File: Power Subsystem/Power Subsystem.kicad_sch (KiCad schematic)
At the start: 8 parts, among them J1 Conn_01x16_Pin, J2 Conn_01x02_Pin, U1 MCP73831-2-OT

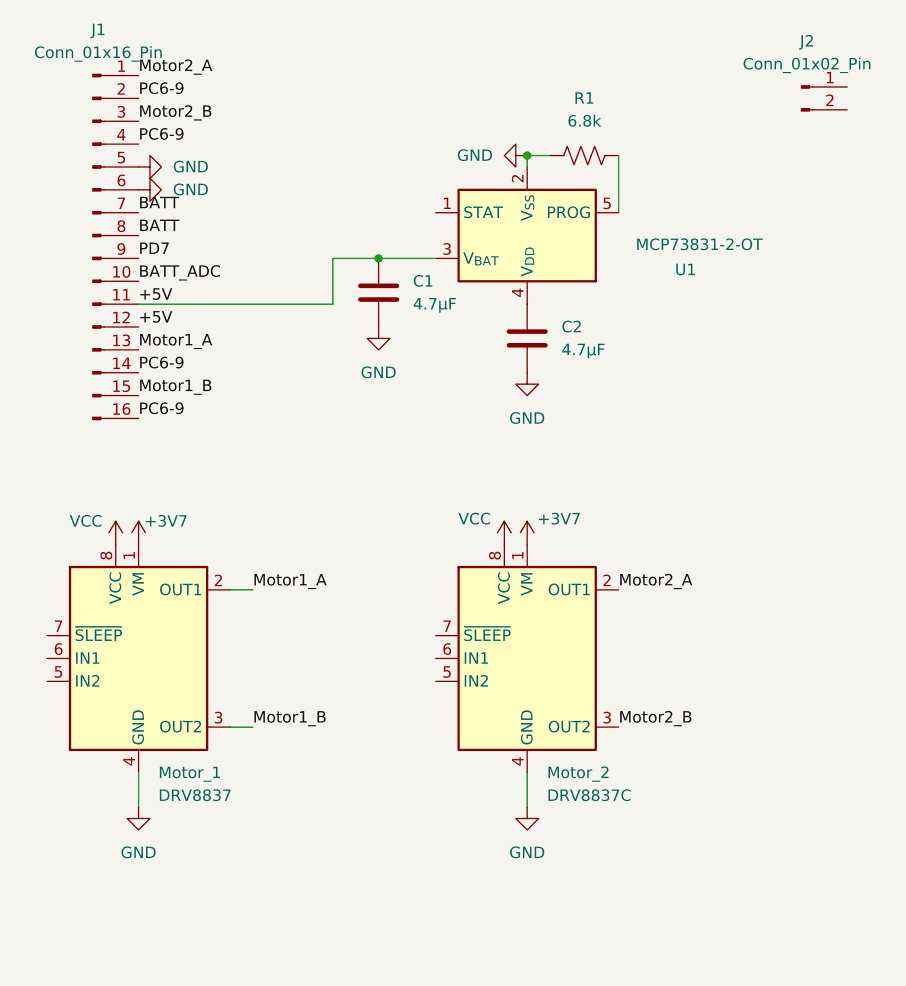
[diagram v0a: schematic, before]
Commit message: Final design (2 errors, 3 warnings)
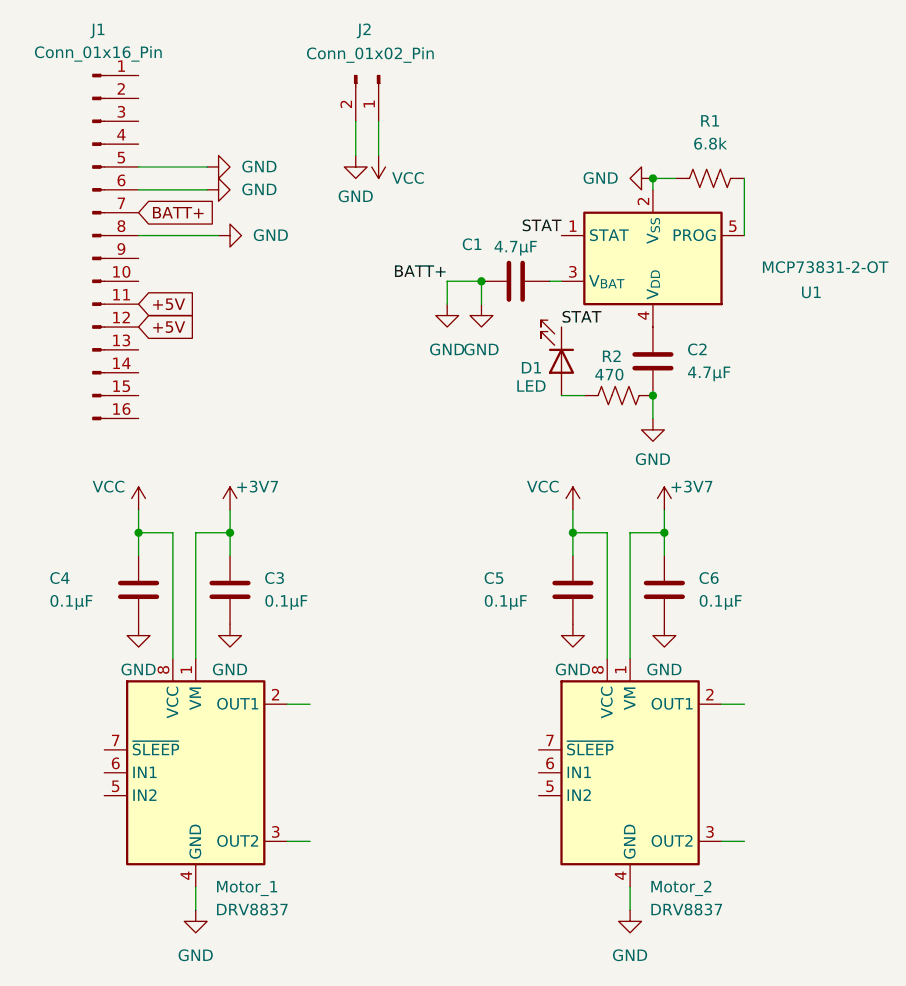
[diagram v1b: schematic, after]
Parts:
- removed Motor_2: DRV8837C, Package_SON:WSON-8-1EP_2x2mm_P0.5mm_EP0.9x1.6mm, symbol Driver_Motor:DRV8837C
- added C3, C4, C5, C6: 0.1µF, Capacitor_THT:C_Radial_D5.0mm_H5.0mm_P2.00mm, symbol Device:C
- added D1: LED, symbol Device:LED
- added Motor_2: DRV8837, Package_SON:WSON-8-1EP_2x2mm_P0.5mm_EP0.9x1.6mm, symbol Driver_Motor:DRV8837
- added R2: 470, symbol Device:R_US
- J2: footprint (none) -> Connector_JST:JST_PH_B2B-PH-K_1x02_P2.00mm_Vertical
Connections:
- net BATT is gone; now on net GND: J1.7 (Pin_7), J1.8 (Pin_8)
- net +3V7: now also C3.1, C6.1, Motor_2.1 (VM)
- net +5V: no longer C1.1, U1.3 (V_{BAT})
- net GND: now also C1.1, J2.2 (Pin_2), C3.2, C4.2, C5.2, C6.2, Motor_2.4 (GND), Motor_2.9 (GND), R2.2; no longer C1.2
- net VCC: now also J2.1 (Pin_1), C4.1, C5.1, Motor_2.8 (VCC)
- net STAT: now reaches U1.1 (STAT)
- net STAT: now also D1.1 (K)
- net BATT_ADC: no longer names the net of J1.10 (Pin_10)
- net Motor1_A: no longer names the net of Motor_1.2 (OUT1)
- net Motor1_A: no longer J1.13 (Pin_13)
- net Motor1_B: no longer names the net of Motor_1.3 (OUT2)
- net Motor1_B: no longer J1.15 (Pin_15)
- net Motor2_A: no longer names the net of J1.1 (Pin_1)
- net Motor2_B: no longer names the net of J1.3 (Pin_3)
- removed net PC6-9: J1.14 (Pin_14), J1.16 (Pin_16), J1.2 (Pin_2), J1.4 (Pin_4)
- net PD7: no longer names the net of J1.9 (Pin_9)
- new net: D1.2 (A), R2.1
- new net: C1.2, U1.3 (V_{BAT})
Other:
- moved on the sheet: C1, C2, J2, Motor_1, R1, U1

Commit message: Most recent Schematic/PCB
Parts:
- removed C5, C6: 0.1µF, Capacitor_THT:C_Radial_D5.0mm_H5.0mm_P2.00mm, symbol Device:C
- added +5V1, +BATT1, GND1, Motor2_B1, Motor_1A1, Motor_1B1, Motor_2A1, PWM1, PWM2, PWM3, PWM4: TestPoint, TestPoint:TestPoint_Keystone_5019_Minature, symbol Connector:TestPoint
- added JP1, JP11, JP2, JP5, JP8: Jumper_2_Open, Jumper:SolderJumper-2_P1.3mm_Open_TrianglePad1.0x1.5mm, symbol Jumper:Jumper_2_Open
- added JP13: Jumper_2_Bridged, Jumper:SolderJumper-2_P1.3mm_Bridged2Bar_RoundedPad1.0x1.5mm, symbol Jumper:Jumper_2_Bridged
- added Q1: PMOS, Package_TO_SOT_SMD:SOT-23, symbol Simulation_SPICE:PMOS
- added R10, R11: 3k, Resistor_SMD:R_0603_1608Metric, symbol Device:R_US
- added R3: 6.8k, Resistor_SMD:R_0603_1608Metric, symbol Device:R_US
- added R4, R5: 470, Resistor_SMD:R_0402_1005Metric, symbol Device:R_US
- added R7, R8: 1.2k, Resistor_SMD:R_0603_1608Metric, symbol Device:R_US
- added SW1: SW_SPST, Button_Switch_SMD:SW_DIP_SPSTx01_Slide_Omron_A6S-110x_W8.9mm_P2.54mm, symbol Switch:SW_SPST
- C1, C2: footprint Capacitor_THT:C_Radial_D5.0mm_H5.0mm_P2.00mm -> Capacitor_SMD:C_0402_1005Metric; LCSC (none) -> C1538
- C3, C4: value 0.1µF -> 100nF; footprint Capacitor_THT:C_Radial_D5.0mm_H5.0mm_P2.00mm -> Capacitor_SMD:C_0402_1005Metric; LCSC (none) -> C1525
- D1: footprint (none) -> LED_THT:LED_D5.0mm
- J2: footprint Connector_JST:JST_PH_B2B-PH-K_1x02_P2.00mm_Vertical -> Connector_JST:JST_PH_S2B-PH-K_1x02_P2.00mm_Horizontal
- Motor_1, Motor_2: LCSC (none) -> C191000
- R1: value 6.8k -> 560; footprint (none) -> Resistor_SMD:R_0603_1608Metric; LCSC (none) -> C23204
- R2: value 470 -> 6.8k; footprint (none) -> Resistor_SMD:R_0603_1608Metric; LCSC (none) -> C23212
- U1: LCSC (none) -> C424093
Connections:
- net +3V7 is gone; now on net +BATT: C3.1, Motor_1.1 (VM), Motor_2.1 (VM)
- net +5V: now also C2.1, U1.4 (V_{DD}), +5V1.1, R4.2, R5.2
- net GND: now also C1.2, GND1.1, JP11.1 (A), JP2.1 (A), R10.1, R3.1, SW1.1 (A); no longer C1.1, J1.7 (Pin_7), J1.8 (Pin_8), R1.1, R2.2
- net Motor1_A: now reaches Motor_1.2 (OUT1)
- net Motor1_A: now also J1.13 (Pin_13), Motor_1A1.1
- net Motor1_B: now reaches Motor_1.3 (OUT2)
- net Motor1_B: now also J1.15 (Pin_15), Motor_1B1.1
- net PWM4: now reaches Motor_1.5 (IN2)
- net PWM4: now also J1.16 (Pin_16), PWM4.1
- net PWM3: now reaches Motor_1.6 (IN1)
- net PWM3: now also J1.14 (Pin_14), PWM3.1
- net +BATT: now reaches Motor_1.7 (~{SLEEP})
- net +BATT: now also C1.1, C4.1, J1.7 (Pin_7), J1.8 (Pin_8), Motor_1.8 (VCC), Motor_2.7 (~{SLEEP}), Motor_2.8 (VCC), U1.3 (V_{BAT}), +BATT1.1, JP1.2 (B), Q1.1 (D), R7.2, R8.2
- net Motor2_A: now reaches J1.1 (Pin_1)
- net Motor2_A: now also Motor_2.2 (OUT1), Motor_2A1.1
- net BATT_ADC: now reaches J1.10 (Pin_10)
- net BATT_ADC: now also JP8.1 (A), R10.2, R11.2, R7.1
- net PWM1: now reaches J1.2 (Pin_2)
- net PWM1: now also Motor_2.6 (IN1), PWM1.1
- net Motor2_B: now reaches J1.3 (Pin_3)
- net Motor2_B: now also Motor_2.3 (OUT2), Motor2_B1.1
- net PWM2: now reaches J1.4 (Pin_4)
- net PWM2: now also Motor_2.5 (IN2), PWM2.1
- net RESV: now reaches J1.9 (Pin_9)
- net at R2.1: now also JP2.2 (B); no longer D1.2 (A)
- net at U1.5 (PROG): now also R2.2, R3.2; no longer R1.2
- removed net VCC: C4.1, J2.1 (Pin_1), Motor_1.8 (VCC), Motor_2.8 (VCC)
- new net: JP5.2 (B), R5.1
- new net: J2.1 (Pin_1), JP1.1 (A), Q1.3 (S), R1.1
- new net: Q1.2 (G), R1.2, SW1.2 (B)
- new net: D1.2 (A), JP13.2 (B)
- new net: JP8.2 (B), R8.1
- new net: JP11.2 (B), R11.1
- new net: JP13.1 (A), JP5.1 (A), R4.1
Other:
- note added: "Charging circuit, using an MCP73831 IC to regulate current/voltage as well as auto shut-off once charging is completed. LED is includedto indicate whether the battery is charging or full."
- note added: "Two DRV8837 ICs used to control motor speed and direction (PWM Interface)"
- company: (none) -> University of Cape Town
- title: (none) -> Micro Mouse Power Subsystem
- moved on the sheet: D1, J1, J2, Motor_1, Motor_2, U1

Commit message: Final Schematic and PCB designs
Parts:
- removed JP1: Jumper_2_Open, Jumper:SolderJumper-2_P1.3mm_Open_TrianglePad1.0x1.5mm, symbol Jumper:Jumper_2_Open
- removed Q1: PMOS, Package_TO_SOT_SMD:SOT-23, symbol Simulation_SPICE:PMOS
- removed R1: 560, Resistor_SMD:R_0603_1608Metric, symbol Device:R_US
- removed SW1: SW_SPST, Button_Switch_SMD:SW_DIP_SPSTx01_Slide_Omron_A6S-110x_W8.9mm_P2.54mm, symbol Switch:SW_SPST
- added JP1: Jumper_2_Bridged, Jumper:SolderJumper-2_P1.3mm_Bridged2Bar_RoundedPad1.0x1.5mm, symbol Jumper:Jumper_2_Bridged
- added SW1: SW_SPDT_312, Custom Footprints:SW-TH_SS-12D10L5, symbol Switch:SW_SPDT_312
- D1: footprint LED_THT:LED_D5.0mm -> LED_SMD:LED_0603_1608Metric; LCSC (none) -> C2286
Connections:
- net +BATT: now also JP1.2 (B)
- net GND: now also SW1.2 (C)
- net at J2.1 (Pin_1): now also SW1.1 (B)
- new net: JP1.1 (A), SW1.3 (A)
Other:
- moved on the sheet: +5V1, +BATT1, C1, C2, C3, C4, D1, GND1, J1, J2, JP11, JP13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
